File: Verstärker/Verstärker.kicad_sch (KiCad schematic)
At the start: 58 parts, among them J3 ACJS-MHOM, J4 NRJ6HM-1, Q1 MJE182G, Q12 MMBT5401, Q13 MMBT5401, Q2 MJE172G, Q3 MMBT5551(RANGE:200-300), Q9 MMBT5551(RANGE:200-300)

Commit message: dru Datei hinnzugefügt. Silcscreen der Testpoitns angepasst.
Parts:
- added GND4, GND5, GND6, GND7: H5, MountingHole:MountingHole_2.2mm_M2_Pad_TopBottom, symbol Mechanical:MountingHole_Pad
- GND1: renamed from H5; value GND -> H5
- GND2: renamed from TP12; value GND -> TP12
- GND3: renamed from H7; value GND -> H7
- IN1: renamed from H2; value IN -> H2
- IN_AMP_B1: renamed from H9; value IN AMP B -> H9
- Input1: renamed from TP5; value Input -> TP5
- OUT1: renamed from H8; value OUT -> H8
- OUT_AMP_B1: renamed from H1; value OUT AMP B -> H1
- Output1: renamed from TP1; value Output -> TP1
- Q12&Q13_E1: renamed from TP9; value TestPoint -> TP9
- Q12_B1: renamed from TP4; value TestPoint -> TP4
- Q12_C1: renamed from TP10; value TestPoint -> TP10
- Q13&Q12_C1: renamed from TP11; value TestPoint -> TP11
- Q13_E1: renamed from TP8; value TestPoint -> TP8
- Q1_E1: renamed from TP2; value Q1 -> TP2
- Q2_E1: renamed from TP3; value Q2 -> TP3
- Q3_C1: renamed from TP6; value TestPoint -> TP6
- Q3_E1: renamed from TP7; value TestPoint -> TP7
- VCC+1: renamed from H3; value VCC + -> H3
- VCC-1: renamed from H4; value VCC - -> H4
- VCC_GND1: renamed from H6; value VCC GND -> H6
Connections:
- net GND: now also GND4.1, GND5.1, GND6.1, GND7.1

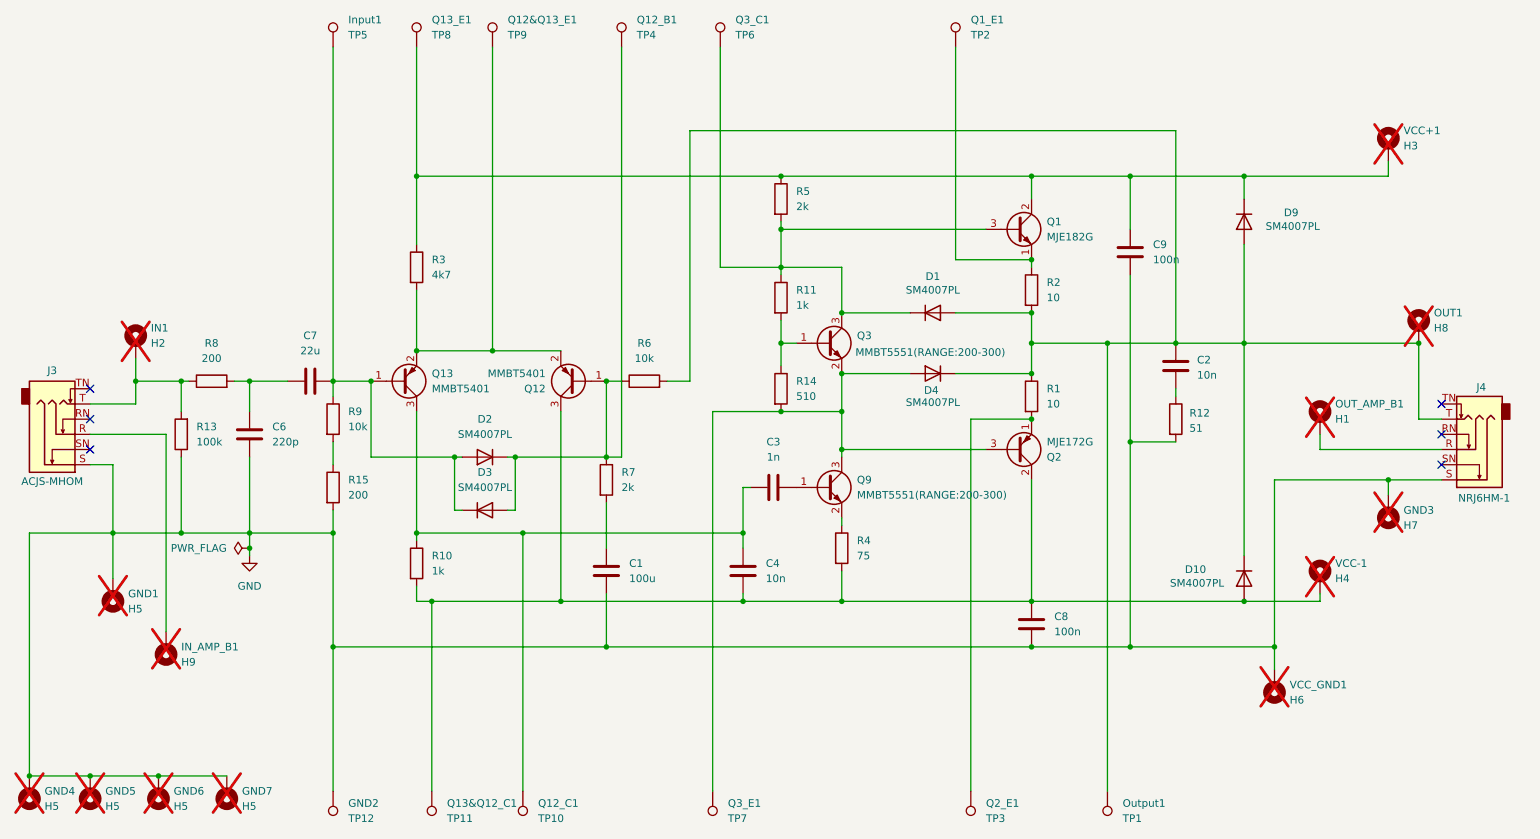
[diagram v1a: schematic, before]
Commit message: do not populate testpoints
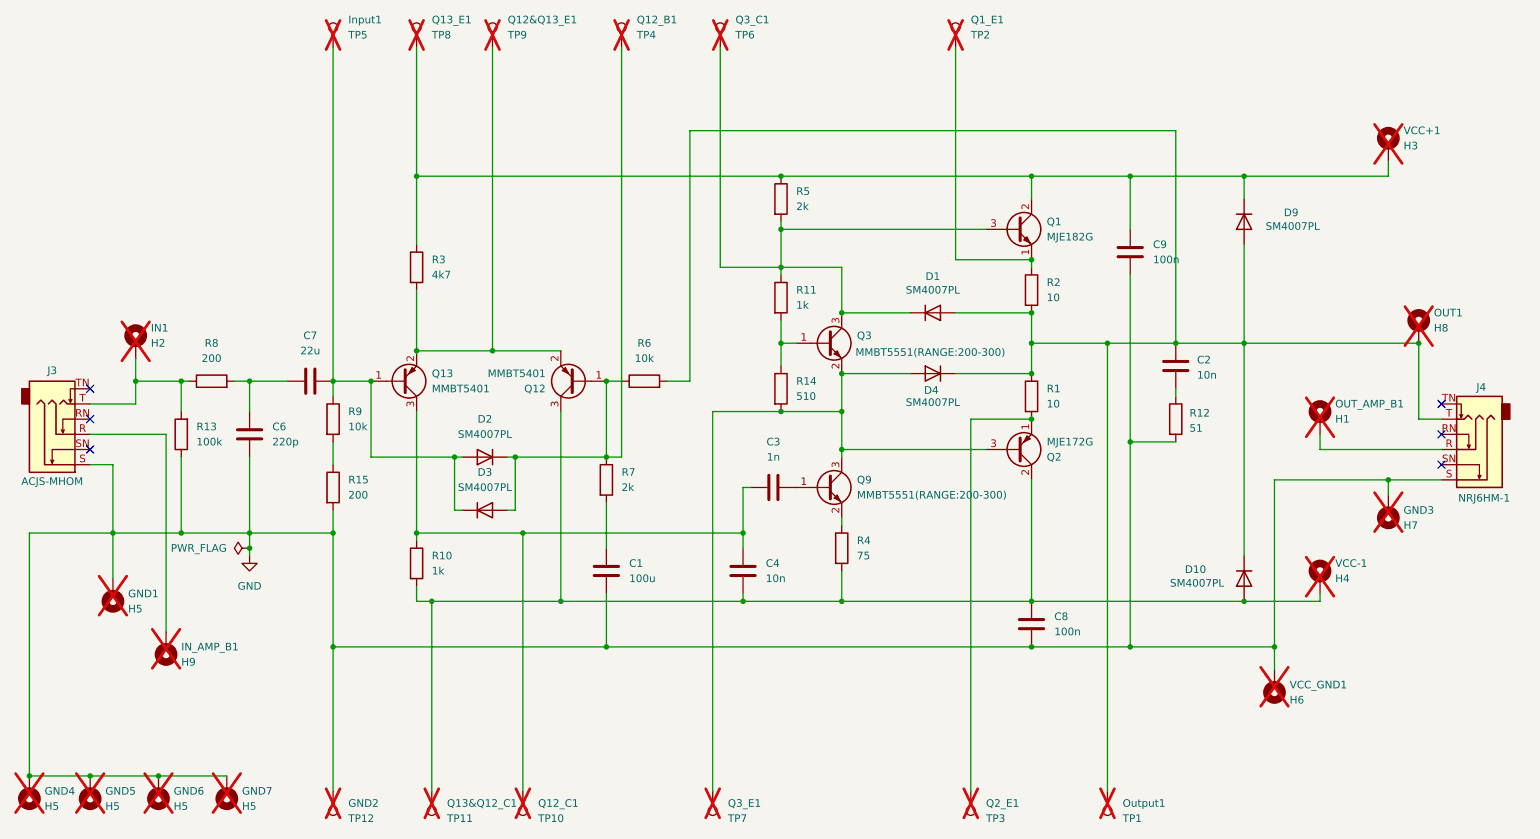
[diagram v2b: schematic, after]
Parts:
- GND2, Input1, Output1, Q12&Q13_E1, Q12_B1, Q12_C1, Q13&Q12_C1, Q13_E1, Q1_E1, Q2_E1, Q3_C1, Q3_E1: now not fitted
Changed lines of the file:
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@@
 		(in_bom yes)
 		(on_board yes)
-		(dnp no)
+		(dnp yes)
 		(fields_autoplaced yes)
 		(property "Reference" "Q3_C1"
@@
 		(in_bom yes)
 		(on_board yes)
-		(dnp no)
+		(dnp yes)
 		(fields_autoplaced yes)
 		(property "Reference" "Q13&Q12_C1"
@@
 		(in_bom yes)
 		(on_board yes)
-		(dnp no)
+		(dnp yes)
 		(fields_autoplaced yes)
 		(property "Reference" "Q12&Q13_E1"
@@
 		(in_bom yes)
 		(on_board yes)
-		(dnp no)
+		(dnp yes)
 		(fields_autoplaced yes)
 		(property "Reference" "Q12_C1"
@@
 		(in_bom yes)
 		(on_board yes)
-		(dnp no)
+		(dnp yes)
 		(fields_autoplaced yes)
 		(property "Reference" "Q3_E1"
@@
 		(in_bom yes)
 		(on_board yes)
-		(dnp no)
+		(dnp yes)
 		(fields_autoplaced yes)
 		(property "Reference" "Input1"
@@
 		(in_bom yes)
 		(on_board yes)
-		(dnp no)
+		(dnp yes)
 		(fields_autoplaced yes)
 		(property "Reference" "GND2"
@@
 		(in_bom yes)
 		(on_board yes)
-		(dnp no)
+		(dnp yes)
 		(fields_autoplaced yes)
 		(property "Reference" "Q2_E1"
@@
 		(in_bom yes)
 		(on_board yes)
-		(dnp no)
+		(dnp yes)
 		(fields_autoplaced yes)
 		(property "Reference" "Output1"
@@
 		(in_bom yes)
 		(on_board yes)
-		(dnp no)
+		(dnp yes)
 		(fields_autoplaced yes)
 		(property "Reference" "Q13_E1"
@@
 		(in_bom yes)
 		(on_board yes)
-		(dnp no)
+		(dnp yes)
 		(fields_autoplaced yes)
 		(property "Reference" "Q12_B1"
@@
 		(in_bom yes)
 		(on_board yes)
-		(dnp no)
+		(dnp yes)
 		(fields_autoplaced yes)
 		(property "Reference" "Q1_E1"

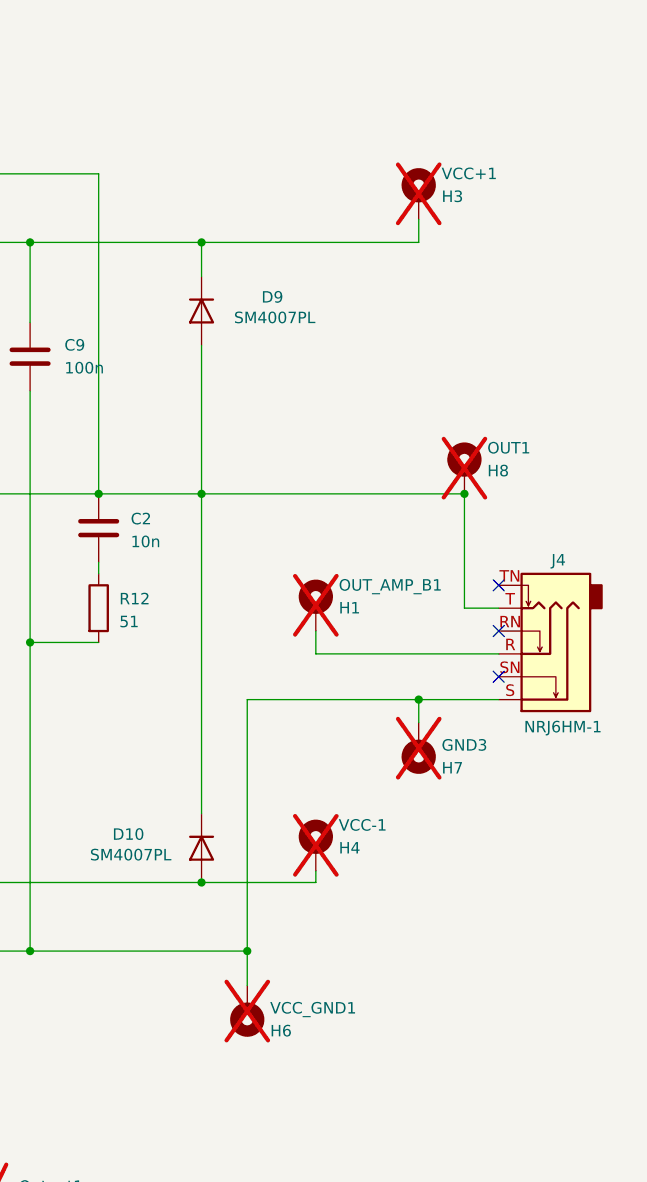
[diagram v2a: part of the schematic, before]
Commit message: Alles auf 10cm Breite geschrumpft. Keine Vias
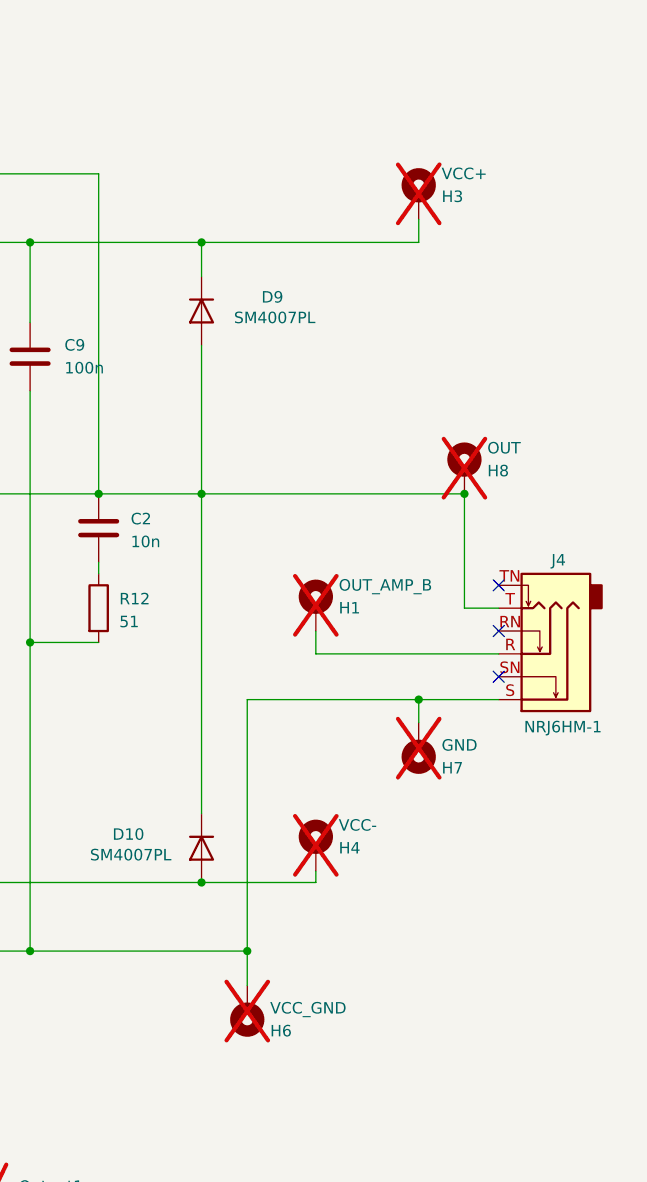
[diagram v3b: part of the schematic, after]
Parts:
- renumbered GND3 to GND, OUT1 to OUT, OUT_AMP_B1 to OUT_AMP_B, VCC+1 to VCC+, VCC-1 to VCC-, VCC_GND1 to VCC_GND
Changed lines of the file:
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@@
 		(dnp yes)
 		(fields_autoplaced yes)
-		(property "Reference" "GND3"
+		(property "Reference" "GND"
 			(at 255.27 101.5999 0)
 			(effects
@@
 			(project ""
 				(path "/e102fd65-1476-4a8b-9749-6e526a3708eb"
-					(reference "GND3")
+					(reference "GND")
 					(unit 1)
 				)
@@
 		(dnp yes)
 		(fields_autoplaced yes)
-		(property "Reference" "OUT1"
+		(property "Reference" "OUT"
 			(at 260.35 68.5799 0)
 			(effects
@@
 			(project ""
 				(path "/e102fd65-1476-4a8b-9749-6e526a3708eb"
-					(reference "OUT1")
+					(reference "OUT")
 					(unit 1)
 				)
@@
 		(dnp yes)
 		(fields_autoplaced yes)
-		(property "Reference" "OUT_AMP_B1"
+		(property "Reference" "OUT_AMP_B"
 			(at 243.84 83.8199 0)
 			(effects
@@
 			(project ""
 				(path "/e102fd65-1476-4a8b-9749-6e526a3708eb"
-					(reference "OUT_AMP_B1")
+					(reference "OUT_AMP_B")
 					(unit 1)
 				)
@@
 		(dnp yes)
 		(fields_autoplaced yes)
-		(property "Reference" "VCC-1"
+		(property "Reference" "VCC-"
 			(at 243.84 110.4899 0)
 			(effects
@@
 			(project ""
 				(path "/e102fd65-1476-4a8b-9749-6e526a3708eb"
-					(reference "VCC-1")
+					(reference "VCC-")
 					(unit 1)
 				)
@@
 		(dnp yes)
 		(fields_autoplaced yes)
-		(property "Reference" "VCC+1"
+		(property "Reference" "VCC+"
 			(at 255.27 38.0999 0)
 			(effects
@@
 			(project ""
 				(path "/e102fd65-1476-4a8b-9749-6e526a3708eb"
-					(reference "VCC+1")
+					(reference "VCC+")
 					(unit 1)
 				)
@@
 		(dnp yes)
 		(fields_autoplaced yes)
-		(property "Reference" "VCC_GND1"
+		(property "Reference" "VCC_GND"
 			(at 236.22 130.8099 0)
 			(effects
@@
 			(project ""
 				(path "/e102fd65-1476-4a8b-9749-6e526a3708eb"
-					(reference "VCC_GND1")
-					(unit 1)
-				)
+					(reference "VCC_GND")
+					(unit 1)
+				)
